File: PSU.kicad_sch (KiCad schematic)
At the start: 37 parts, among them J17 Barrel_Jack_Switch, J18 USB_C_Receptacle_USB2.0_16P, Q78 2N7002, Q79 2N7002, U14 USB PD等快充协议受电芯片-CH224K-ESSOP10, U78 TL431DBZ

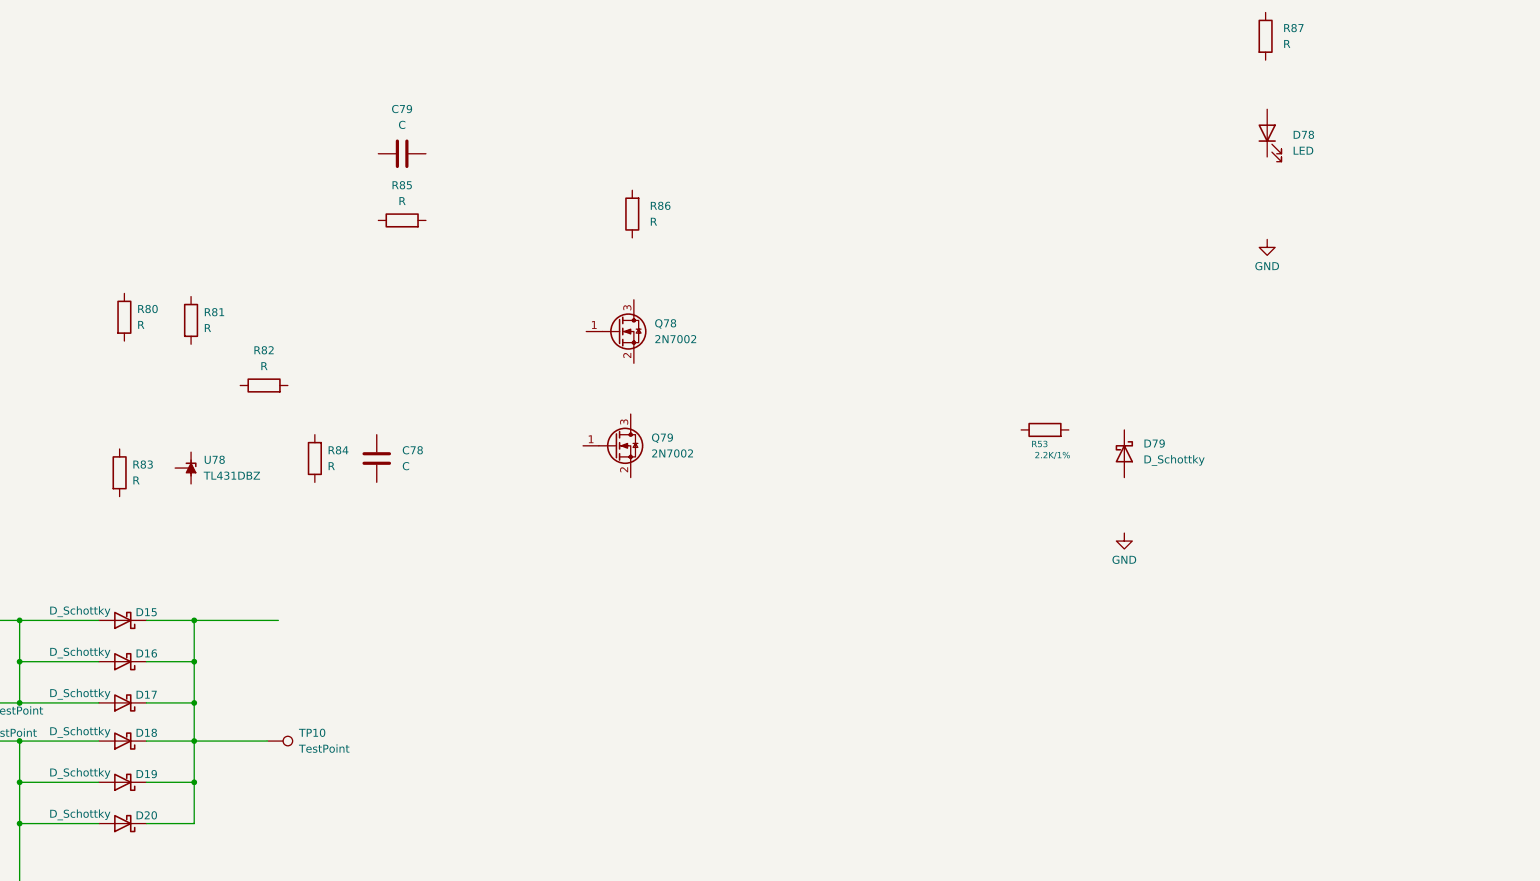
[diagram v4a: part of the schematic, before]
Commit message: Implimented the sub circuit for the PCIe x4 lanes Power for PCIe x4 0VP@13.86V
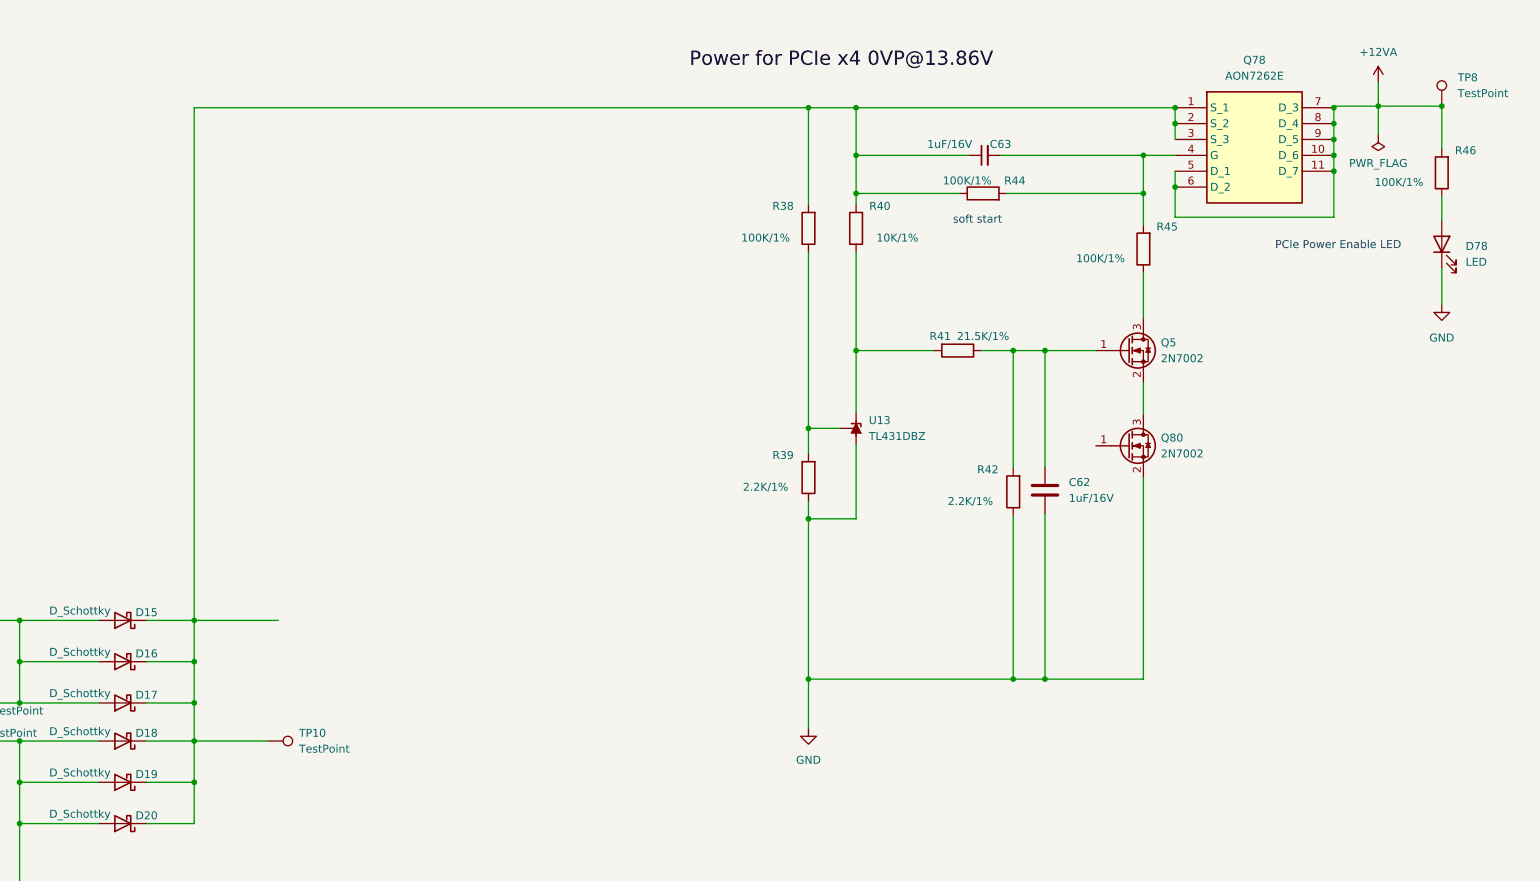
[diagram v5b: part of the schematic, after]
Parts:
- removed C78, C79: C, symbol Device:C
- removed D79: D_Schottky, symbol Device:D_Schottky
- removed Q78, Q79: 2N7002, Package_TO_SOT_SMD:SOT-23, symbol Transistor_FET:2N7002
- removed R53: 2.2K/1%, A_HDJ_Library:R_0402_1005Metric, symbol Device:R
- removed R80, R81, R82, R83, R84, R85, R86, R87: R, symbol Device:R
- removed U78: TL431DBZ, Package_TO_SOT_SMD:SOT-23, symbol Reference_Voltage:TL431DBZ
- added C62: 1uF/16V, A_HDJ_Library:C_0402_1005Metric, symbol Device:C
- added C63: 1uF/16V, A_HDJ_Library:C_0402_1005Metric, symbol Device:C_Small
- added Q5: 2N7002, A_HDJ_Library:SOT-23, symbol Transistor_FET:2N7002
- added Q78: AON7262E, A_HDJ_Library:MOSFET_PDFN8_3.3x3.3, symbol A_HDJ_Library:AON7262E
- added Q80: 2N7002, Package_TO_SOT_SMD:SOT-23, symbol Transistor_FET:2N7002
- added R38, R44, R45, R46: 100K/1%, symbol Device:R
- added R39, R42: 2.2K/1%, symbol Device:R
- added R40: 10K/1%, symbol Device:R
- added R41: 21.5K/1%, symbol Device:R
- added TP8: TestPoint, symbol Connector:TestPoint
- added U13: TL431DBZ, A_HDJ_Library:SOT-23, symbol Reference_Voltage:TL431DBZ
- D78: footprint (none) -> A_HDJ_Library:LED_0603_1608Metric
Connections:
- net GND: now also D78.1 (K), C62.2, Q80.2 (S), R39.1, R42.1, U13.3 (A)
- net at D15.1 (K), D16.1 (K), D17.1 (K)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: now also C63.1, Q78.1 (S_1), Q78.2 (S_2), Q78.3 (S_3), R38.2, R40.2, R44.1
- net at D78.2 (A): now also R46.1
- new net: R40.1, R41.2, U13.1 (K)
- new net: R38.1, R39.2, U13.2 (REF)
- new net: Q5.2 (S), Q80.3 (D)
- new net: C62.1, Q5.1 (G), R41.1, R42.2
- new net: Q5.3 (D), R45.1
- new net: C63.2, Q78.4 (G), R44.2, R45.2
- new net +12VA: Q78.10 (D_6), Q78.11 (D_7), Q78.5 (D_1), Q78.6 (D_2), Q78.7 (D_3), Q78.8 (D_4), Q78.9 (D_5), R46.2, TP8.1
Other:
- note added: "PCIe Power Enable LED"
- note added: "soft start"

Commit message: Added the 3.3v and the 5V power regulator sub circuits in the PSU schematic sheet
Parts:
- added C64, C65, C67, C68, C74, C75, C76, C77, C78, C79, C80, C81, C82, C83: 22uF/10V, A_HDJ_Library:C_0603_1608Metric, symbol Device:C_Small
- added C70, C71: 100uF/50V, A_HDJ_Library:C_0603_1608Metric, symbol Device:C_Small
- added D22: LED, A_HDJ_Library:LED_0603_1608Metric, symbol Device:LED
- added D79: +3V3 Izt=5mA, Diode_SMD:D_SOD-323, symbol Device:D_Schottky
- added JP78: Jumper_3_Bridged12, symbol Jumper:Jumper_3_Bridged12
- added L1, L2: 2.2UH/4.3A, A_HDJ_Library:L_Sunlord_SWPA4020S, symbol Device:L
- added Q79: 2N7002, A_HDJ_Library:SOT-23, symbol Transistor_FET:2N7002
- added R47: 1k/1%, A_HDJ_Library:R_0402_1005Metric, symbol Device:R
- added R49, R58: 10k/1%, A_HDJ_Library:R_0402_1005Metric, symbol Device:R
- added R51 (x2): 100k/1%, A_HDJ_Library:R_0402_1005Metric, symbol Device:R
- added R52 (x2): 2.2k/1%, A_HDJ_Library:R_0402_1005Metric, symbol Device:R
- added R57: 75k/1%, A_HDJ_Library:R_0402_1005Metric, symbol Device:R
- added R59: 21.5k/1%, A_HDJ_Library:R_0402_1005Metric, symbol Device:R
- added R60: 4.7k/1%, A_HDJ_Library:R_0402_1005Metric, symbol Device:R
- added R80: R, symbol Device:R
- added TP13, TP5, TP6: TestPoint, symbol Connector:TestPoint
- added U15, U16: LM2734X, Package_TO_SOT_SMD:TSOT-23, symbol Regulator_Switching:LM2734X
- R36: value 1k/1% -> 10k/1%
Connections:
- net GND: now also C64.1, C65.2, C67.2, C68.1, C74.2, C75.2, C76.2, C77.2, C78.2, C79.2, C80.2, C81.2, C82.2, C83.2, D79.2 (A), Q79.2 (S), R49.2, R51.1, R58.1, R60.1, U15.2 (GND), U16.2 (GND)
- net PWR_C_D-: now also J18.A6 (D+), J18.B6 (D+)
- net VDC: now reaches C63.1, D15.1 (K), D16.1 (K), D17.1 (K), D18.1 (K), D19.1 (K), D20.1 (K), Q78.1 (S_1), Q78.2 (S_2), Q78.3 (S_3), R38.2, R40.2, R44.1, TP10.1
- net VDC: now also C64.2, C65.1, C67.1, C68.2, R52.2, U15.5 (VIN), U16.5 (VIN)
- new net: JP78.2 (C), R51.2
- new net: D22.1 (K), Q79.3 (D)
- new net: D22.2 (A), R52.2
- new net: R59.1, R60.2
- new net: Q79.1 (G), R47.1, R49.1
- new net: C70.1, L1.1, U15.6 (SW)
- new net: C70.2, U15.1 (BOOST)
- new net: R57.1, R58.2, U15.3 (FB)
- new net: C71.1, L2.1, U16.6 (SW)
- new net +3.3V: C75.1, C77.1, C79.1, C81.1, C83.1, L2.2, R52.1, R59.2, TP6.1
- new net +5V: C74.1, C76.1, C78.1, C80.1, C82.1, L1.2, R57.2, TP5.1
- new net PWR_EN: R51.1, R51.2, U15.4 (EN), U16.4 (EN)
- new net SLS_S3: JP78.3 (B)
- new net VPullup: D79.1 (K), R52.1, TP13.1
- new net ~{PWR_LED}/~{PSON}: JP78.1 (A), R47.2
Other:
- moved on the sheet: C61, C62, C63, D10, D11, D12, D13, D14, D15, D16, D17, D18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

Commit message: Added the power and the restet button sub circuits to the psu shematic sheet
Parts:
- removed R80: R, symbol Device:R
- added C66, C69: 1uF/16V, A_HDJ_Library:C_0402_1005Metric, symbol Device:C_Small
- added D21, D25: ESD9B5.0ST5G, A_HDJ_Library:D_0402_1005Metric, symbol Diode:ESD9B5.0ST5G
- added R48, R55: 100R/1%, A_HDJ_Library:R_0402_1005Metric, symbol Device:R
- added R50, R56: 10k/1%, A_HDJ_Library:R_0402_1005Metric, symbol Device:R
- added SW1, SW2: SW_Push, A_HDJ_Library:SW_Push_6x6x6, symbol Switch:SW_Push
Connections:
- net +3.3V: now also R50.1, R56.1
- net GND: now also C66.2, C69.2, D21.1 (A1), SW1.2, SW2.2
- net at U16.1 (BOOST): now also C71.2
- new net: C66.1, D21.2 (A2), R48.1, R50.2, SW1.1
- new net: C69.1, D25.2 (A2), R55.1, R56.2, SW2.1
- new net ~{PWR_SWD}: R48.2
- new net ~{RST_SWD}: R55.2
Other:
- note added: "12V DC Input(12V 6A-10A)"
- note added: "15V PD Input"
- note added: "LattePanda Mu has integrated pull-up resistors."
- note added: "Power for PCIe x4 OVP@13.86V"
- note added: "SY8253ADC 23V 3A 500kHz"
- note added: "Vout=0.6*(21.5+4.7)/4.7=3.446V"
- moved on the sheet: C61, C62, C63, C64, C65, C67, C68, C70, C71, C74, C75, C76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

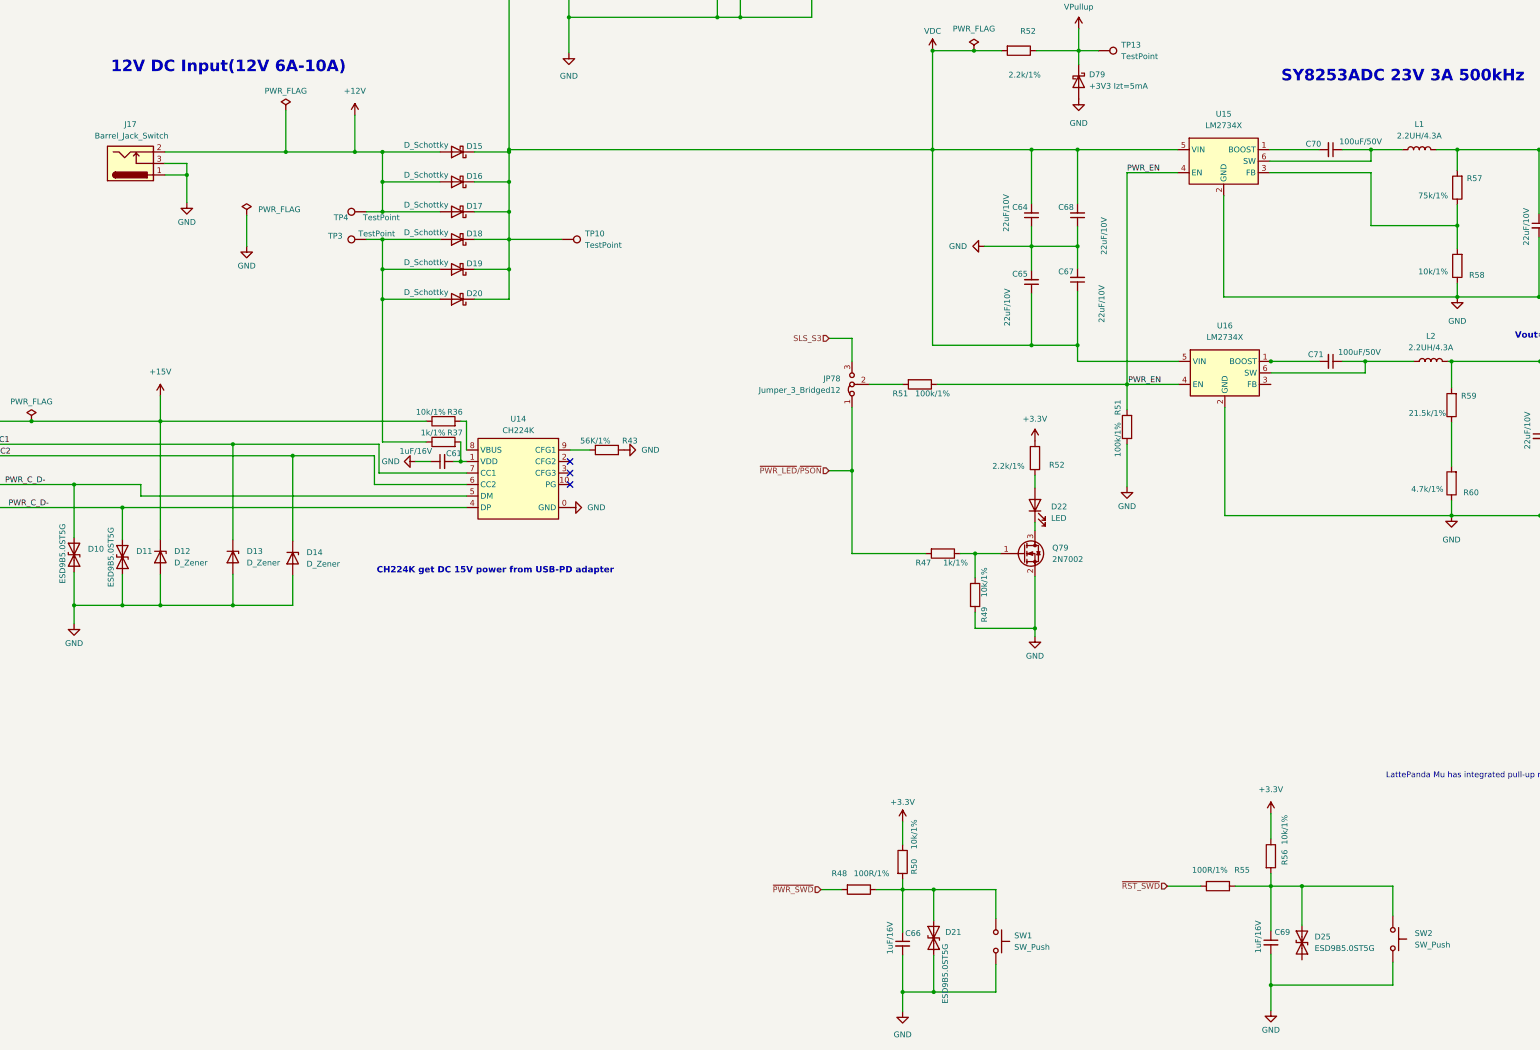
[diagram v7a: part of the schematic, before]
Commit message: Fixed the grid settings and now need to fix all the unconnected wires
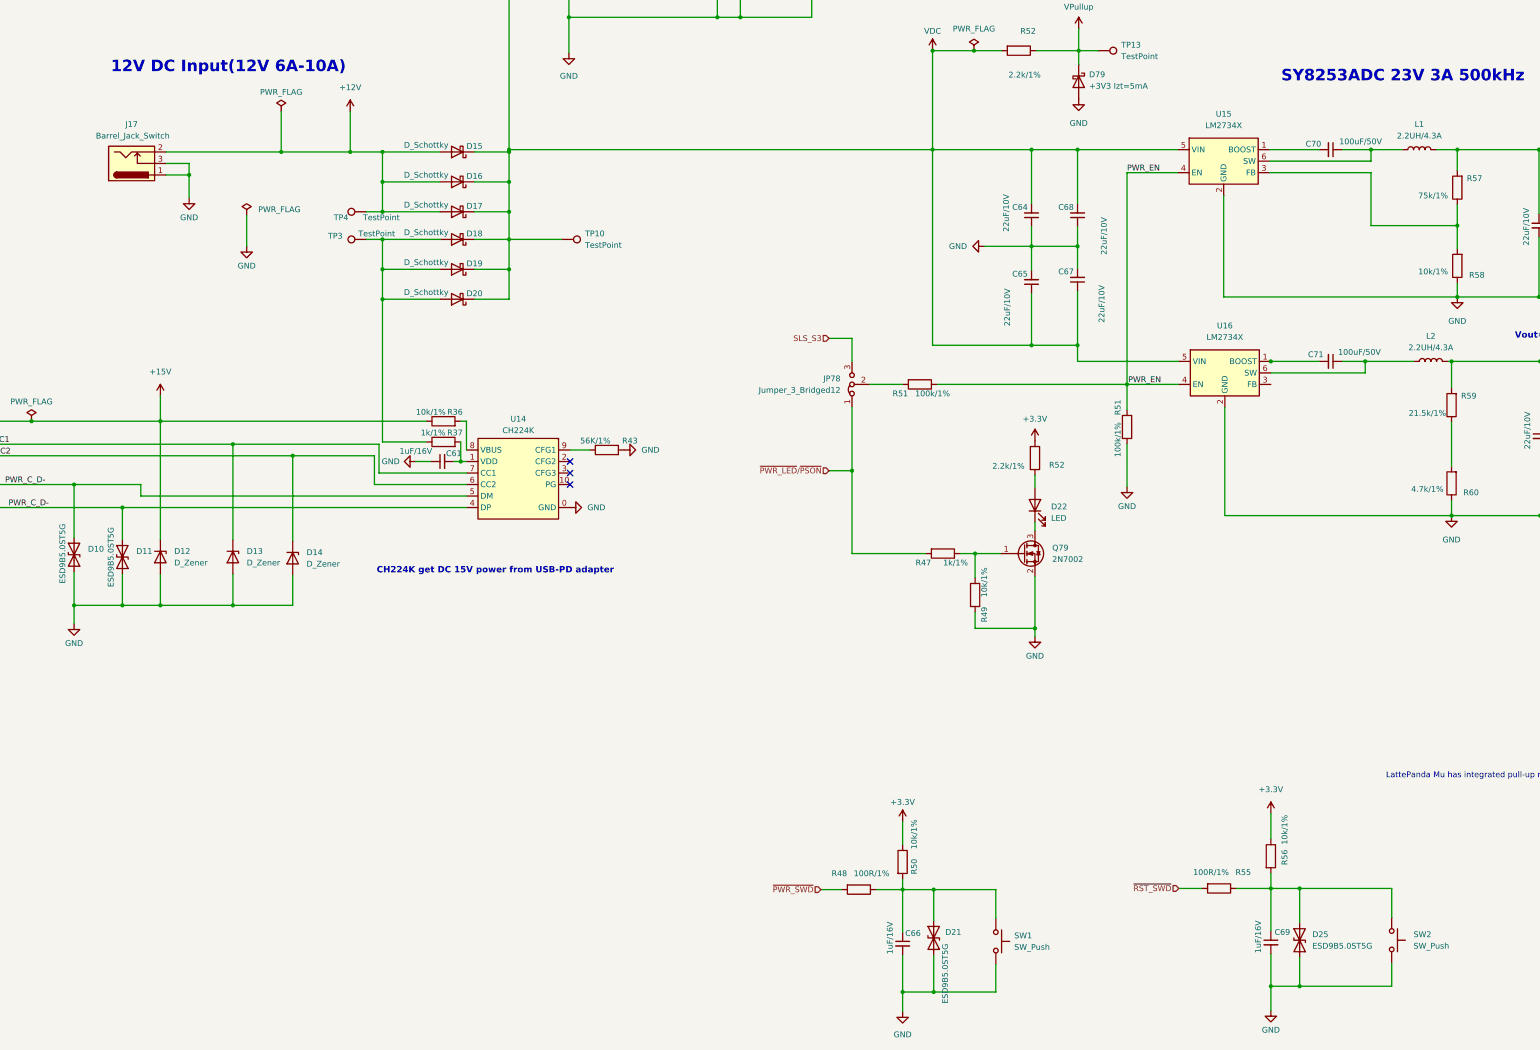
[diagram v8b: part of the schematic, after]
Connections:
- net GND: now also D25.1 (A1)
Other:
- moved on the sheet: D25, R55
